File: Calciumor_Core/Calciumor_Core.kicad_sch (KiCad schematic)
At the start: 127 parts, among them J1 OLED, J2 USB_C_Main, Q2 2SC4116, Q3 2SC4116, SW1 SW_Push, SW10 SW_Push, SW11 SW_Push, SW12 SW_Push, SW13 SW_Push, SW14 SW_Push, SW15 SW_Push, SW16 SW_Push, SW17 SW_Push, SW18 SW_Push, SW19 TMHU27, SW2 SW_Push, SW20 Power_SW, SW21 Program, SW22 Reset, SW3 SW_Push, SW4 RotaryEncoder_Switch, SW5 SW_Push, SW6 SW_Push, SW7 SW_Push, SW8 SW_Push, SW9 SW_Push, U1 LM324APT, U2 NJM12877F25, U3 ESP32-S3-WROOM-1-N16R8, U4 MCP73831-2-OT, U5 BD5229G-1, U6 NC7SV157, U7 FT231XS, U8 XC6194AA03ER-G, U9 AE-XC9306-3V3

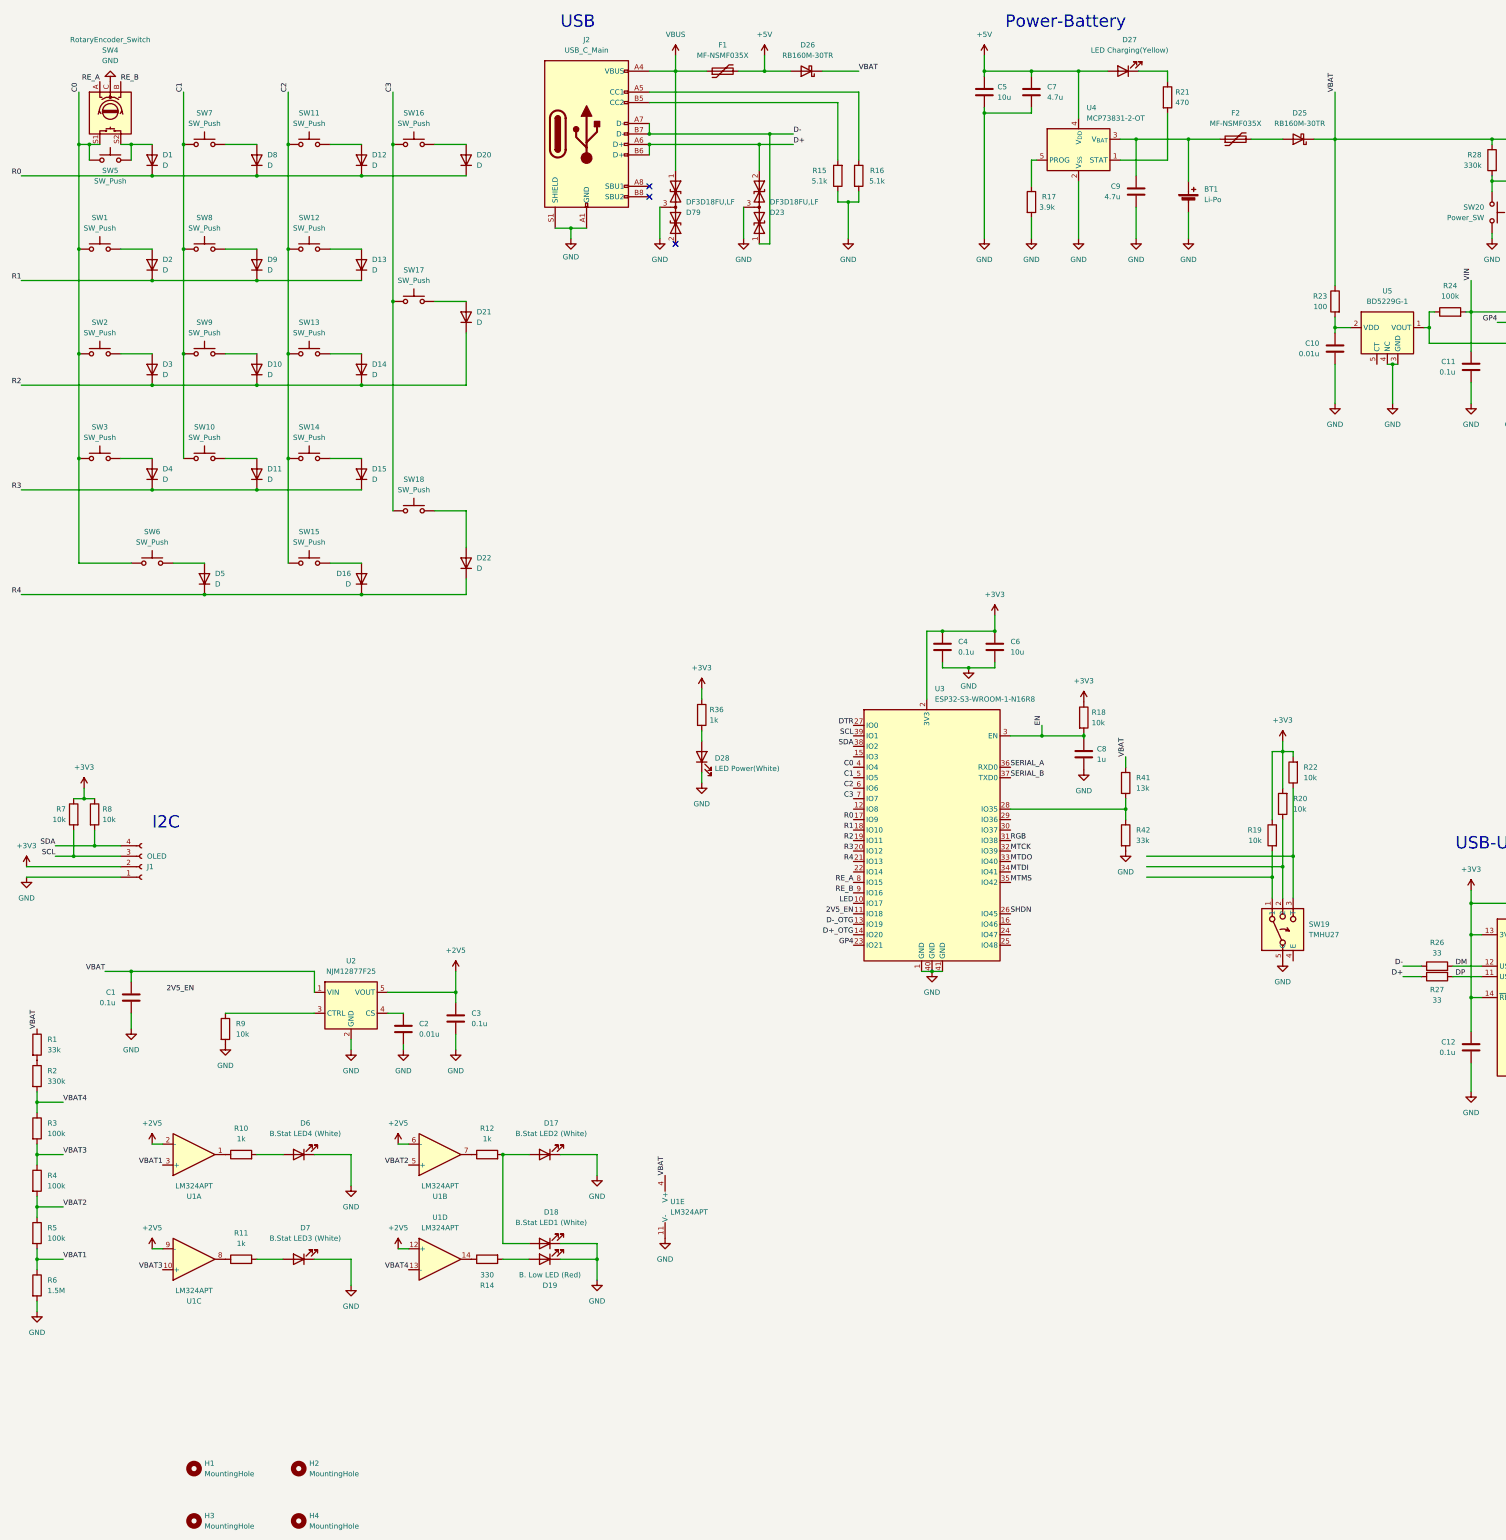
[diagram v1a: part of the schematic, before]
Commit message: Adjust Patterns and Pastes
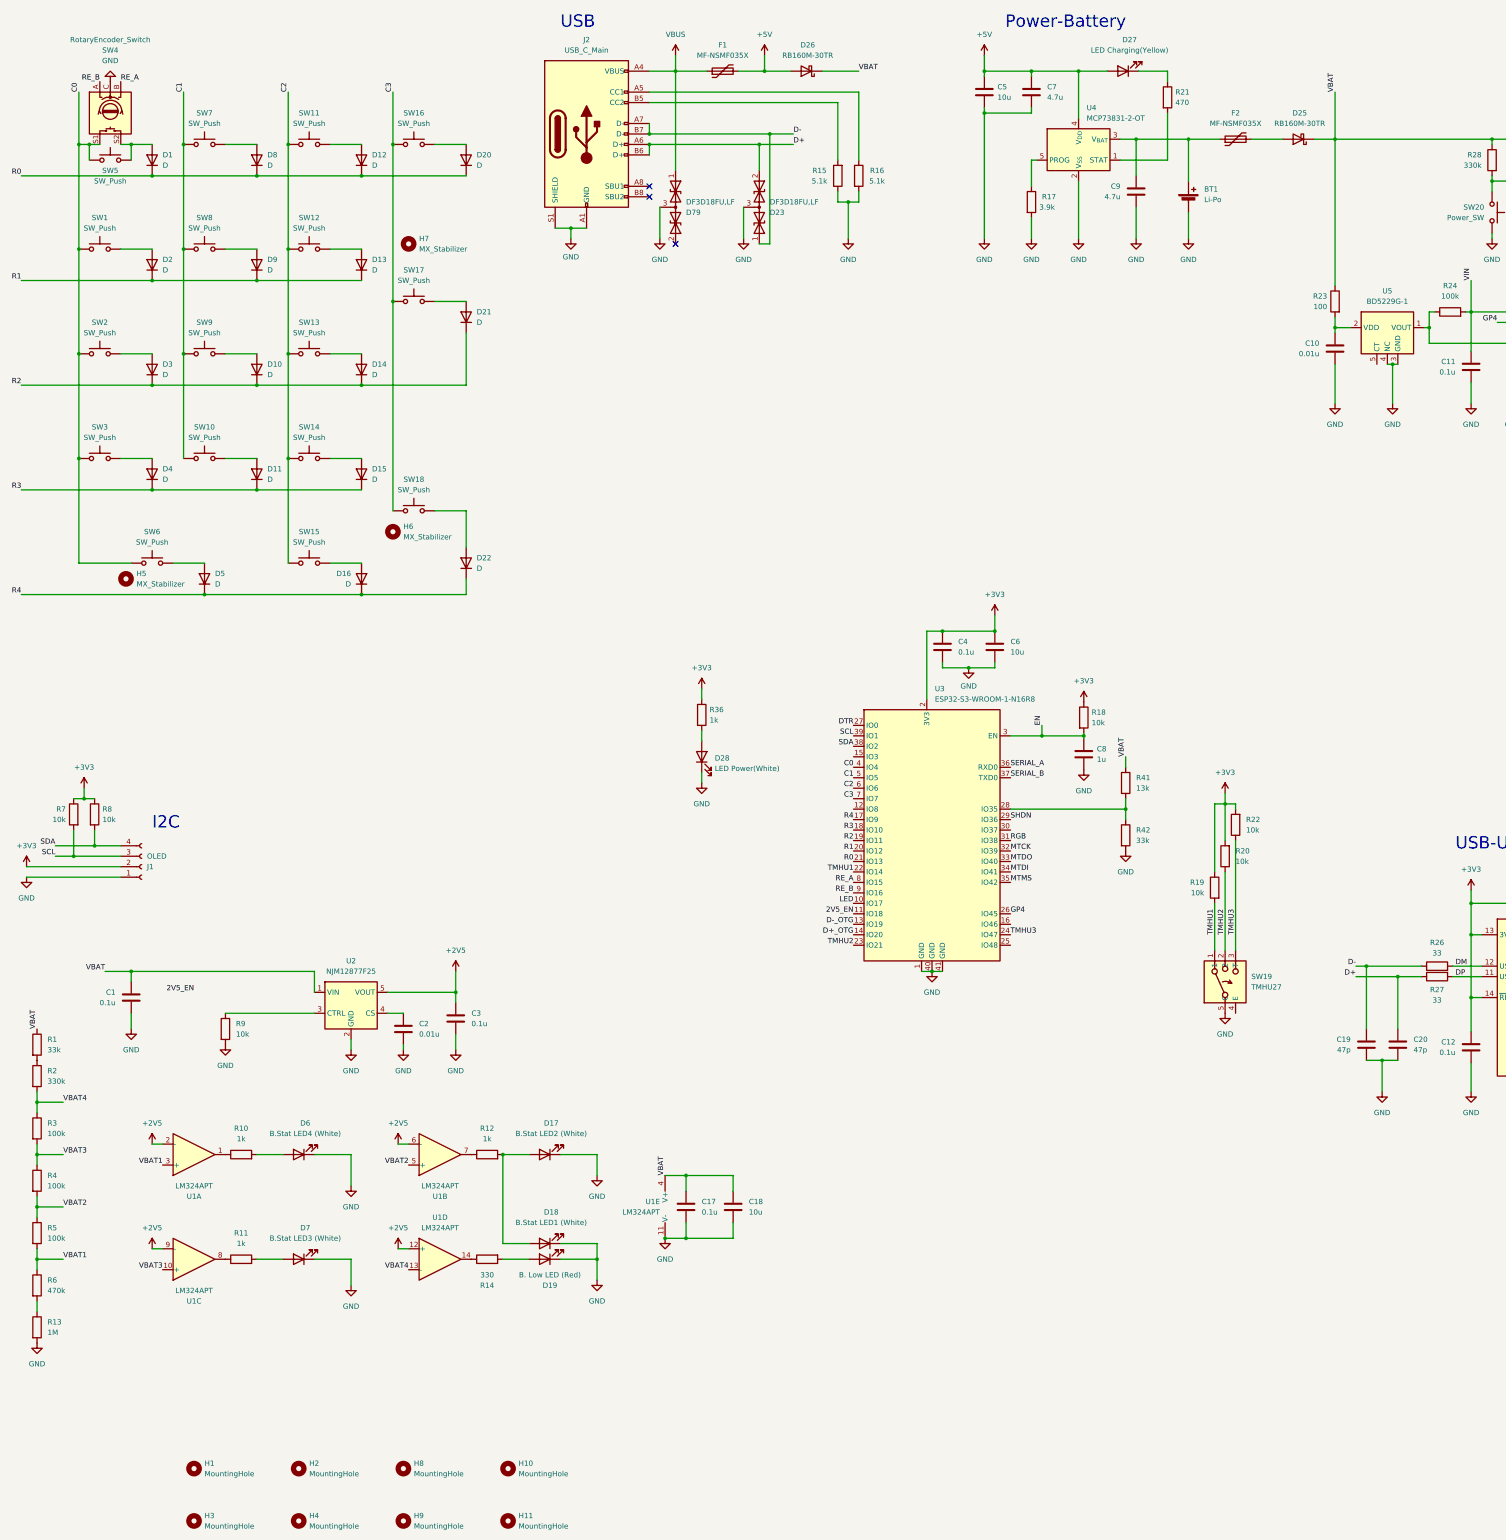
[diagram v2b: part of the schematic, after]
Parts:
- added C17: 0.1u, Capacitor_SMD:C_0402_1005Metric, symbol Device:C
- added C18: 10u, Capacitor_SMD:C_0805_2012Metric, symbol Device:C
- added C19, C20: 47p, Capacitor_SMD:C_0402_1005Metric, symbol Device:C
- added H10, H11, H8, H9: MountingHole, MountingHole:MountingHole_2.2mm_M2, symbol Mechanical:MountingHole
- added H5, H6, H7: MX_Stabilizer, PCM_Mounting_Keyboard_Stabilizer:Stabilizer_Cherry_MX_2.00u, symbol Mechanical:MountingHole
- added R13: 1M, Resistor_SMD:R_0603_1608Metric, symbol Device:R
- C13: LCSC C307331 -> C1523
- C5, C6: LCSC C15850 -> C440198
- D1, D10, D11, D12, D13, D14, D15, D16, D2, D20, D21, D22, D3, D4, D5, D8, D9: footprint Ultramarine-2:SOD-123 -> Diode_SMD:D_SOD-123
- D17, D18, D28, D6, D7: LCSC C2290 -> (none)
- D19: LCSC C2286 -> (none)
- D27: LCSC C72038 -> (none)
- R14: LCSC C11702 -> C25104
- R2: LCSC C22807 -> C23137
- R28: footprint Resistor_SMD:R_0402_1005Metric -> Resistor_SMD:R_0603_1608Metric
- R3, R4, R5: LCSC C25779 -> C25741
- R42: LCSC C22967 -> C25779
- R6: value 1.5M -> 470k
- U7: LCSC C89607 -> C132160
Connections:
- net C3: now also SW17.1, SW18.1; no longer SW17.2, SW18.2
- net D+: now also C20.1
- net D-: now also C19.1
- net GND: now also C17.2, C18.2, C19.2, C20.2, R13.2; no longer R6.2
- net GP4: now also U3.26 (IO45); no longer U3.23 (IO21)
- net R0: now also U3.21 (IO13); no longer U3.17 (IO9)
- net R1: now also U3.20 (IO12); no longer U3.18 (IO10)
- net R3: now also U3.18 (IO10); no longer U3.20 (IO12)
- net R4: now also U3.17 (IO9); no longer U3.21 (IO13)
- net RE_A: now also SW4.B; no longer SW4.A
- net RE_B: now also SW4.A; no longer SW4.B
- net SHDN: now also U3.29 (IO36); no longer U3.26 (IO45)
- net VBAT: now also C17.1, C18.1
- net TMHU1: now reaches R19.2, SW19.1
- net TMHU1: now also U3.22 (IO14)
- net TMHU2: now reaches R20.1, SW19.2
- net TMHU2: now also U3.23 (IO21)
- net at D22.2 (A): now also SW18.2; no longer SW18.1
- net at D21.2 (A): now also SW17.2; no longer SW17.1
- net TMHU3: now reaches R22.1, SW19.3 (T)
- net TMHU3: now also U3.24 (IO47)
- new net: R13.1, R6.2
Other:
- moved on the sheet: R19, R20, R22, SW19

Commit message: Fixed 2V5 Power supply
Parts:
- removed D19: B. Low LED (Red), LED_SMD:LED_0603_1608Metric, symbol Device:LED
- removed H1, H3, H4: MountingHole, MountingHole:MountingHole_2.2mm_M2, symbol Mechanical:MountingHole
- removed R9: 10k, Resistor_SMD:R_0402_1005Metric, symbol Device:R
- added JP1: Jumper, Jumper:SolderJumper-3_P2.0mm_Open_TrianglePad1.0x1.5mm, symbol Jumper:SolderJumper_3_Open
- BT1, D26, D27, F1, F2, H10, H11, H6, J1, SW1, SW10, SW11, SW12, SW13, SW14, SW15, SW16, SW17, SW18, SW19, SW2, SW20, SW21, SW22, SW3, SW4, SW5, SW6, SW7, SW8, SW9, U2, U3, U4, U5, U9: now not fitted
- D10: renamed from D6; now not fitted
- D11: renamed from D7; now not fitted
- D20: renamed from D17; now not fitted
- D21: renamed from D18; now not fitted
- D23: renamed from D79; now not fitted
- D24: renamed from D28; now not fitted
- D25: renamed from D23; now not fitted
- D28: renamed from D25; now not fitted
- H1: renamed from H5; now not fitted
- H4: renamed from H2; now not fitted
- H7: renamed from H8; now not fitted
- H8: renamed from H9; now not fitted
- H9: renamed from H7; now not fitted
- Q1: renamed from Q2; now not fitted
- Q2: renamed from Q3; now not fitted
- R18: renamed from R17; now not fitted
- R7: renamed from R13; LCSC C26083 -> C22935
- U7: renamed from U6; LCSC (none) -> C184123
- renumbered C8 to C10, C9 to C11, C10 to C12, C19 to C13, C20 to C14, C11 to C15, C12 to C16, C13 to C17, C14 to C18, C15 to C19, C16 to C20, C17 to C4, C18 to C5, C4 to C6, C5 to C7, C6 to C8, C7 to C9, D20 to D17, D21 to D18, D22 to D19, D8 to D6, D9 to D7, D10 to D8, D11 to D9, R10 to R11, R11 to R12, R12 to R13, R36 to R15, R15 to R16, R16 to R17, R18 to R19, R41 to R20, R42 to R21, R21 to R22, R19 to R23, R20 to R24, R22 to R25, R23 to R26, R26 to R27, R27 to R28, R24 to R29, R28 to R30, R25 to R31, R30 to R32, R29 to R33, R31 to R34, R32 to R35, R33 to R36, R34 to R37, R35 to R38, R37 to R39, R38 to R40, R7 to R8, R8 to R9, U7 to U6
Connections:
- net VBAT: now also U2.3 (CTRL), JP1.1 (A); no longer D26.1 (K)
- net VIN: now also JP1.3 (B)
- net at R14.2: now also D21.2 (A)
- net at D20.2 (A), R13.2: no longer D21.2 (A)
- new net: D26.1 (K), JP1.2 (C)
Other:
- moved on the sheet: C1

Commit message: add 5V power source
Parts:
- removed BT1: Li-Po, Connector_JST:JST_PH_S2B-PH-K_1x02_P2.00mm_Horizontal, symbol Device:Battery_Cell
- removed J1: OLED, Connector_PinHeader_2.54mm:PinHeader_1x04_P2.54mm_Horizontal, symbol Connector:Conn_01x04_Socket
- added C21: 0.1u, Capacitor_SMD:C_0402_1005Metric, symbol Device:C
- added J1: Conn_01x07_Pin, Connector_JST:JST_PH_S6B-PH-SM4-TB_1x06-1MP_P2.00mm_Horizontal, symbol Connector:Conn_01x07_Pin
- added J4: NeoPixel, Connector_JST:JST_PH_S4B-PH-SM4-TB_1x04-1MP_P2.00mm_Horizontal, symbol Connector:Conn_01x05_Socket
- added J5: Li-Po(PH_S2B_SMD), Connector_JST:JST_PH_S2B-PH-SM4-TB_1x02-1MP_P2.00mm_Horizontal, symbol Connector:Conn_01x03_Socket
- added J6: Conn_01x05_Pin, Connector_JST:JST_PH_S4B-PH-SM4-TB_1x04-1MP_P2.00mm_Horizontal, symbol Connector:Conn_01x05_Pin
- added U10: AE-XC9306-5V, Calciumor:AE-XC9306-3V3, symbol Calciumor:AE-XC9306-3V3
- D26, D28: value RB160M-30TR -> SS2040FL
- U8: value XC6194AA03ER-G -> XC6194AA05ER-G
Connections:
- net +3V3: now also J1.5 (Pin_5), J6.3 (Pin_3)
- net +5V: now also C4.1, C5.1, U1.4 (V+), J4.2 (Pin_2), U10.3 (VOUT); no longer C7.1, C9.1, D26.2 (A), D27.2 (A), F1.2, U4.4 (V_{DD})
- net GND: now also C21.2, J1.6 (Pin_6), J1.MP (Pin_7), J4.3 (Pin_3), J4.MP (Pin_5), J5.2 (Pin_2), J5.MP (Pin_3), J6.4 (Pin_4), J6.MP (Pin_5), U10.2 (GND), U10.5 (GND)
- net LED: now also J4.4 (Pin_4)
- net PG: now also U10.4 (EN)
- net RGB: now also J4.1 (Pin_1)
- net SCL: now also J1.4 (Pin_4), J6.2 (Pin_2)
- net SDA: now also J1.3 (Pin_3), J6.1 (Pin_1)
- net VIN: now also C21.1, U10.1 (VIN)
- net at C11.1, F2.1, U4.3 (V_{BAT}): now also J5.1 (Pin_1)
- net TM_OUT: now reaches U3.15 (IO3)
- net TM_OUT: now also J1.1 (Pin_1)
- net TM_CLK: now reaches U3.16 (IO46)
- net TM_CLK: now also J1.2 (Pin_2)
- net VBAT renamed +BATT
- net +BATT: no longer C4.1, C5.1, U1.4 (V+)
- new net: C7.1, C9.1, D26.2 (A), D27.2 (A), F1.2, U4.4 (V_{DD})
- no-connect marks 4 -> 5
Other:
- moved on the sheet: C1, C18, C2, C3, U2, U9
